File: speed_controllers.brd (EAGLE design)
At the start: 147.3 x 147.3 mm, 9 parts

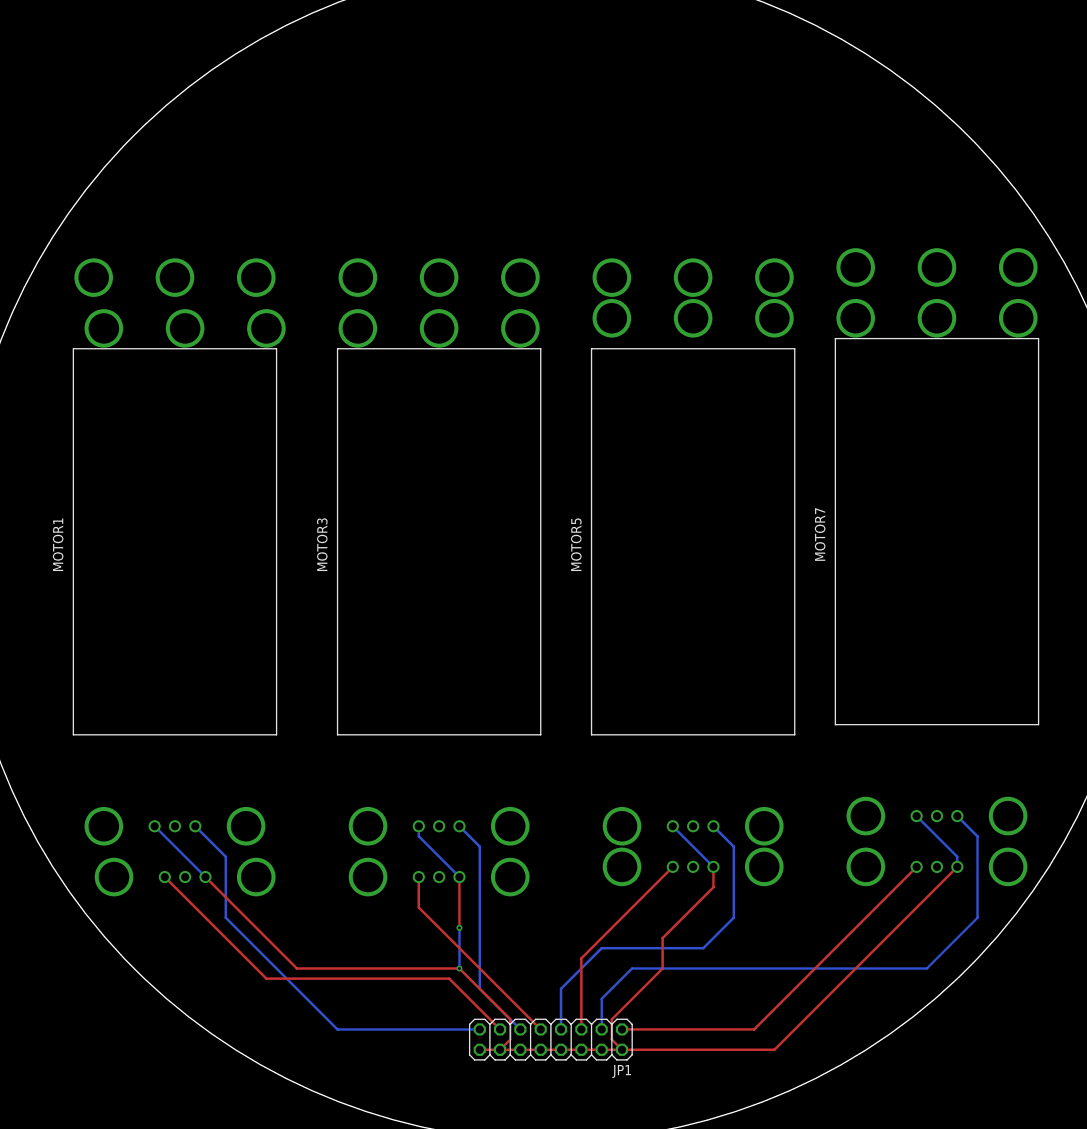
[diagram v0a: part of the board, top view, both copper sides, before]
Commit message: Redid ESC boards
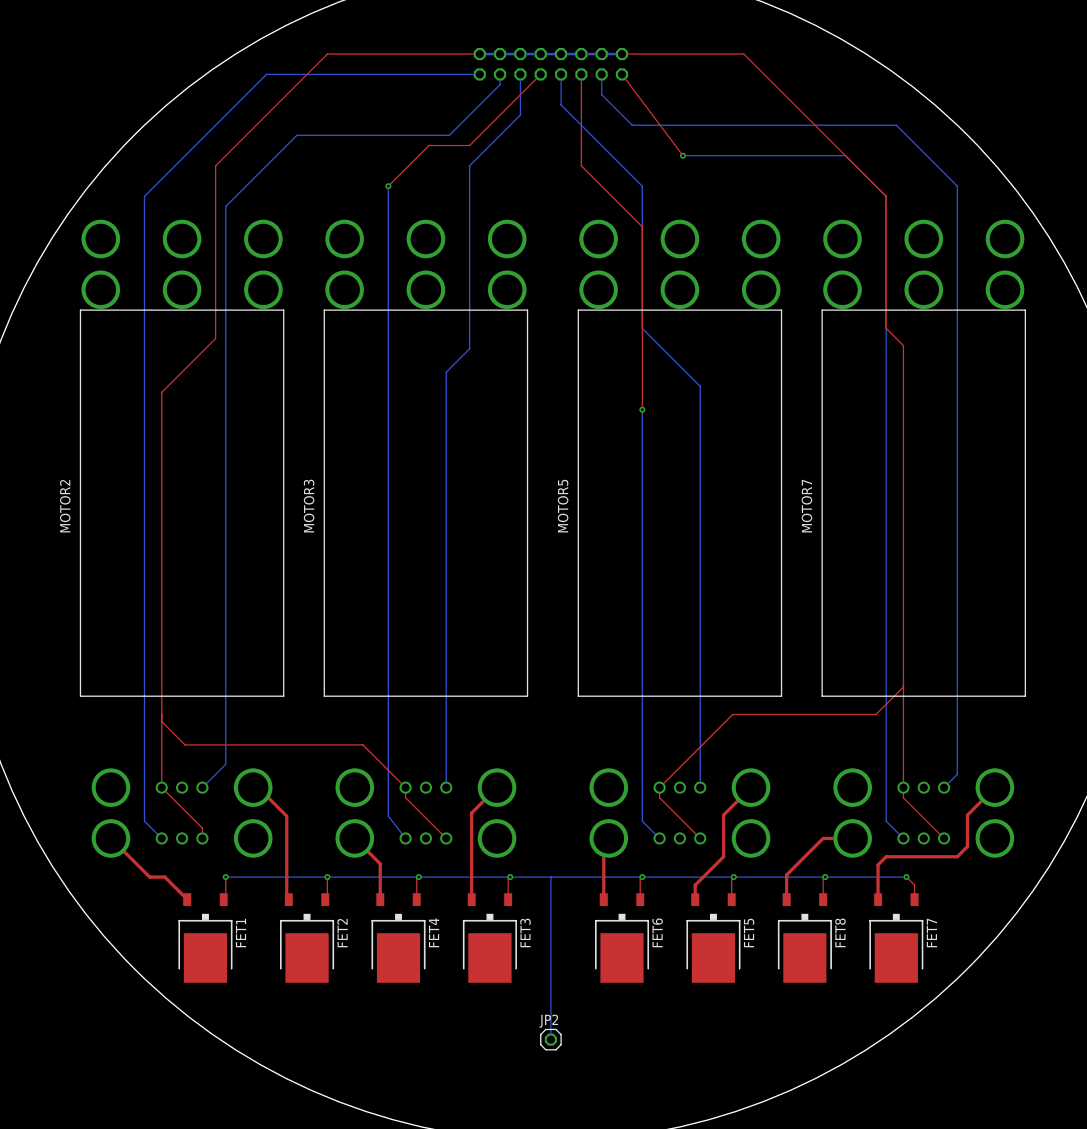
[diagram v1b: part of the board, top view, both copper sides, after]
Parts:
- added FET1, FET2, FET3, FET4, FET5, FET6, FET7, FET8: AOD403, auv:TO252
- added JP2: (no value), auv:1X01
- moved JP1 121.9 mm to (0.00, 61.0), flipped to the bottom, turned to 0 degrees
- moved MOTOR2 11.2 mm to (-46.1, 7.37), flipped to the top
- moved MOTOR4 5.10 mm to (-15.6, 1.02)
- moved MOTOR3 5.10 mm to (-15.6, 7.37)
- moved MOTOR5 5.10 mm to (16.1, 7.37)
- moved MOTOR6 3.92 mm to (16.1, 1.02)
- moved MOTOR7 3.92 mm to (46.6, 7.37)
- moved MOTOR8 3.92 mm to (46.6, 1.02)
- moved MOTOR1 1.76 mm to (-46.1, 1.02), flipped to the bottom
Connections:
- new net N$10: FET1.S, MOTOR1.VIN
- new net N$12: FET2.S, MOTOR2.VIN
- new net N$13: FET3.S, MOTOR3.VIN
- new net N$14: FET4.S, MOTOR4.VIN
- new net N$15: FET5.S, MOTOR5.VIN
- new net N$16: FET6.S, MOTOR6.VIN
- new net N$17: FET7.S, MOTOR7.VIN
- new net N$18: FET8.S, MOTOR8.VIN
- new net N$20: FET1.G, FET2.G, FET3.G, FET4.G, FET5.G, FET6.G, FET7.G, FET8.G, JP2.1
- net VCC: now also FET1.D, FET2.D, FET3.D, FET4.D, FET5.D, FET6.D, FET7.D, FET8.D; no longer MOTOR1.VIN, MOTOR2.VIN, MOTOR3.VIN, MOTOR4.VIN, MOTOR5.VIN, MOTOR6.VIN, MOTOR7.VIN, MOTOR8.VIN
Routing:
- net N$9: track 192.1 -> 357.0 mm, vias 2 -> 0
- net N$20: track 0.00 -> 129.1 mm, vias 0 -> 8
- net N$4: track 25.4 -> 107.1 mm, vias 0 -> 1
- net N$1: track 50.5 -> 129.4 mm
- net N$8: track 45.2 -> 121.4 mm, vias 0 -> 1
- net N$6: track 25.1 -> 99.6 mm, vias 0 -> 1
- net N$2: track 49.8 -> 115.7 mm
- net N$3: track 28.6 -> 93.0 mm
- net N$7: track 68.8 -> 127.6 mm
- net N$5: track 42.8 -> 96.4 mm
- net N$17: track 0.00 -> 25.3 mm
- net N$15: track 0.00 -> 16.9 mm
- net N$12: track 0.00 -> 16.2 mm
- net N$13: track 0.00 -> 15.3 mm
- net N$18: track 0.00 -> 13.2 mm
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
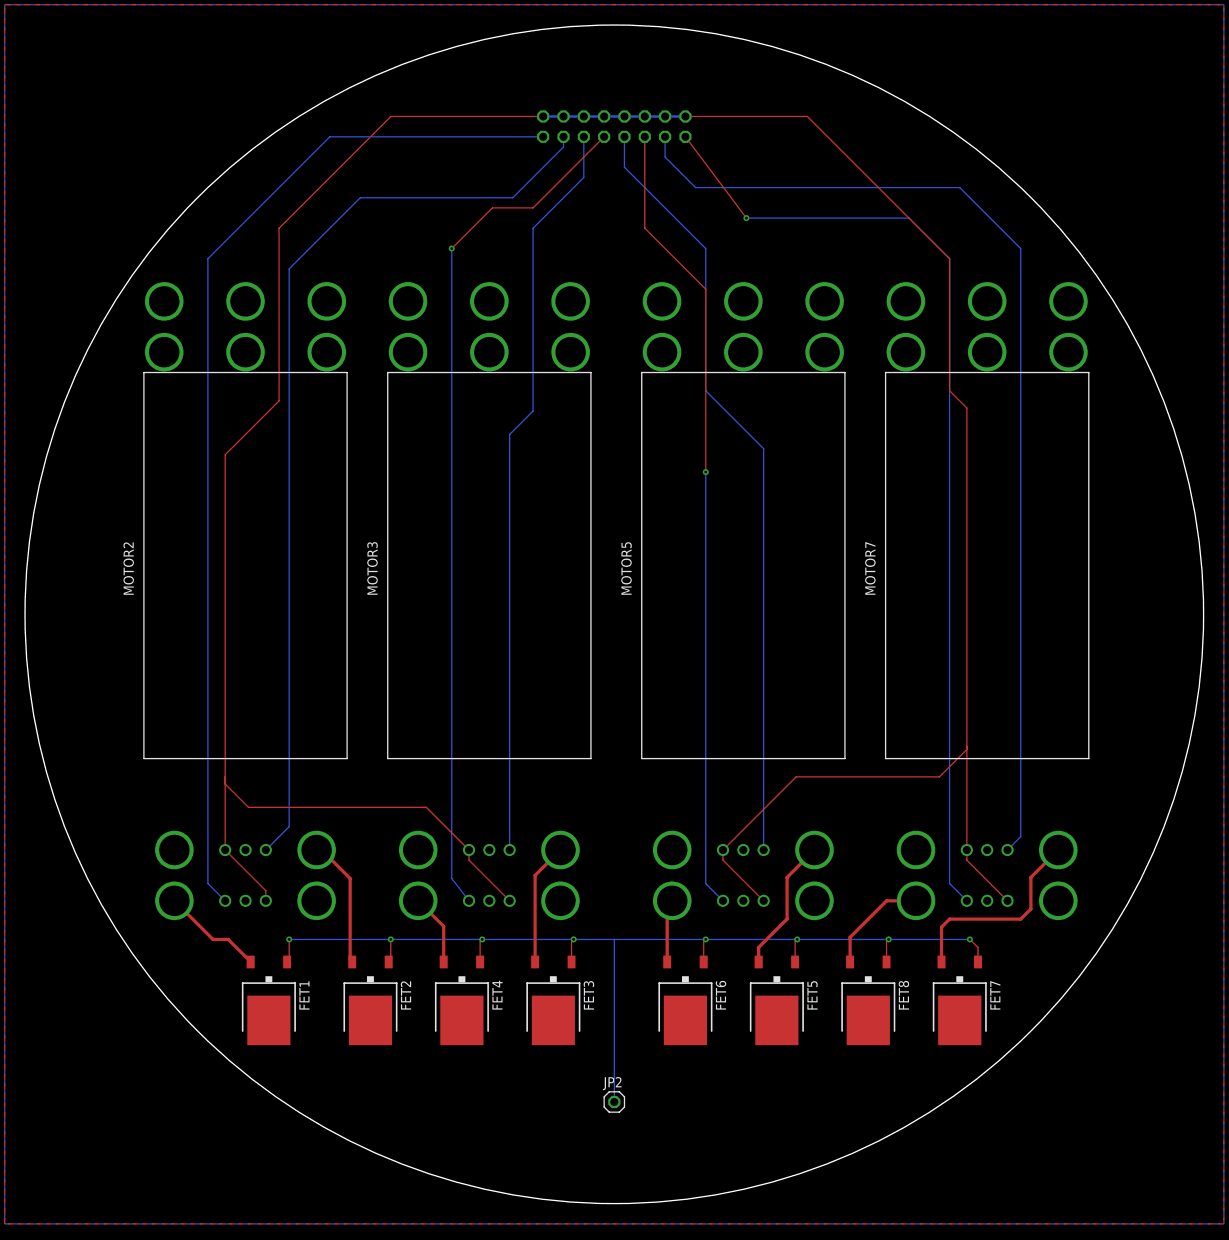
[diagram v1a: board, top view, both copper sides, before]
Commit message: ESC Board
Features:
* 8 ESC's
* XT60 battery connector P-Channel mosfets for kill switch
* Hall effect kill switch
* LED Kill switch indicators
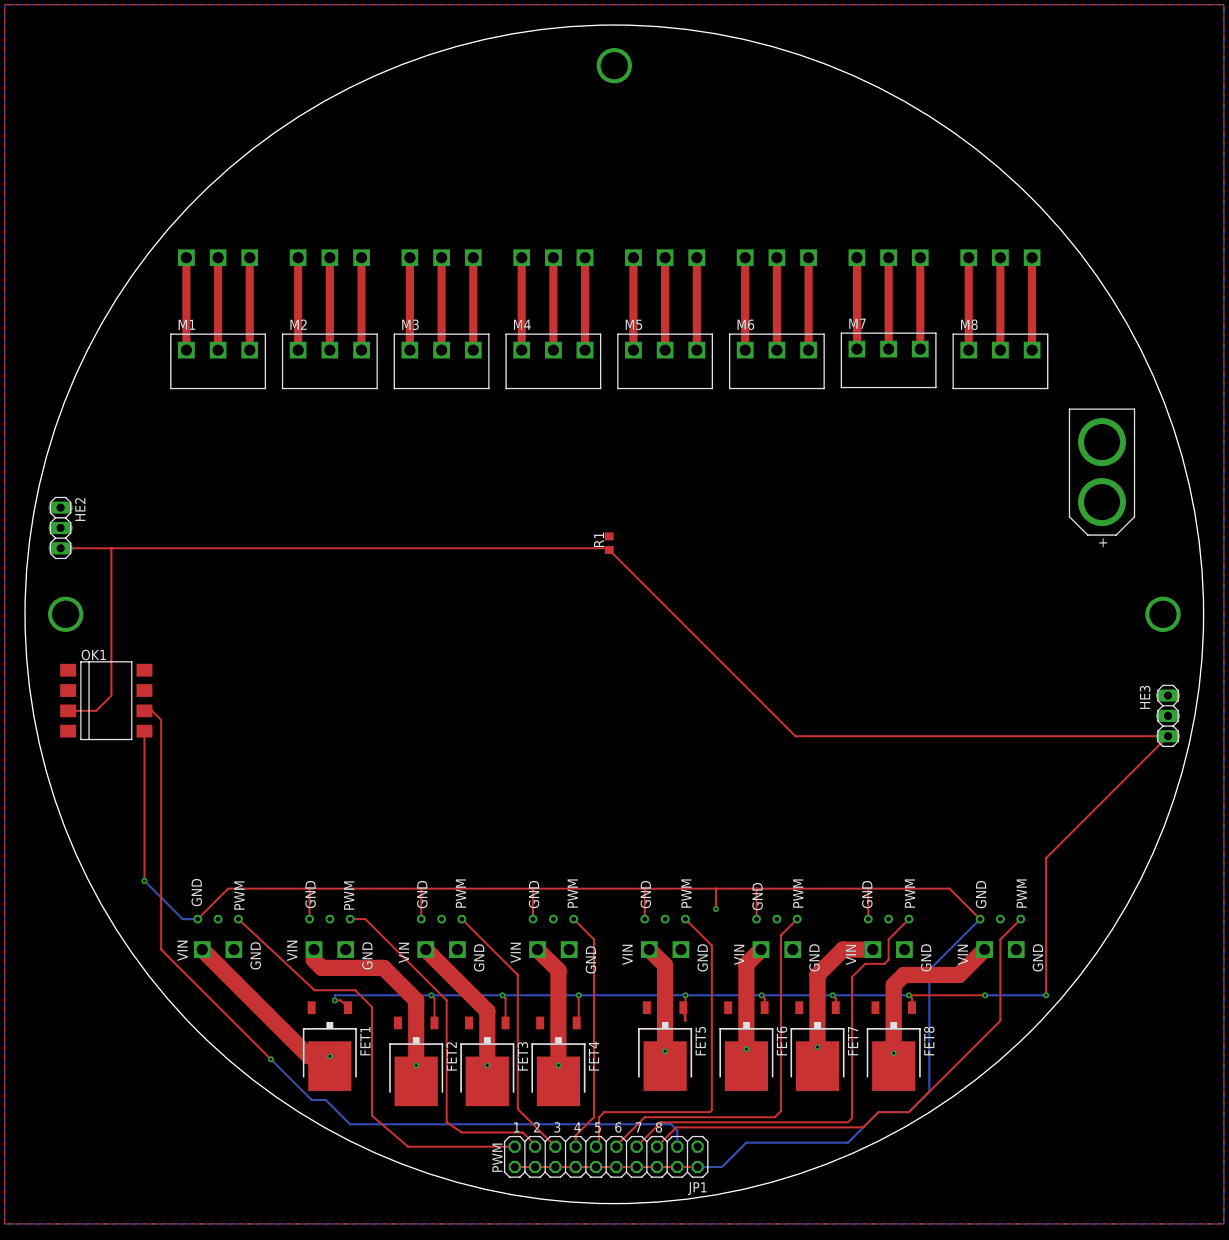
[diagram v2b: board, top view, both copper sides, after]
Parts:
- removed JP2: (no value), auv:1X01
- added HE2, HE3: (no value), auv:1X03
- added LED1, LED2, LED3, LED4, LED5, LED6, LED7, LED8: LED, auv:LED-0603
- added M1, M2, M3, M4, M5, M6, M7, M8: TE-1-1123723-3, auv:TE-1-1123723-3
- added OK1: 6N137SMD, auv:DIL8-SMD
- added R1: 10k, auv:R0603
- added R2, R3, R4, R5, R6, R7, R8, R9: 1k, auv:R0603
- added U$1: XT-60, auv:XT-60
- JP1: device auv:2X08 -> auv:2X10
- moved JP1 128.8 mm to (-1.02, -67.8), flipped to the top, turned to 180 degrees
- moved FET7 18.7 mm to (25.4, -54.0)
- moved FET5 15.1 mm to (6.35, -54.0)
- moved FET4 14.3 mm to (-6.99, -55.9)
- moved MOTOR7 13.7 mm to (34.3, 1.27), flipped to the bottom
- moved MOTOR2 12.2 mm to (-35.6, 1.27), flipped to the bottom
- moved MOTOR5 11.5 mm to (6.35, 1.27), flipped to the bottom
- moved FET3 11.2 mm to (-15.9, -55.9)
- moved FET2 9.53 mm to (-24.8, -55.9)
- moved FET6 9.53 mm to (16.5, -54.0)
- moved FET1 9.53 mm to (-35.6, -54.0)
- moved MOTOR3 8.53 mm to (-21.6, 1.27), flipped to the bottom
- moved MOTOR4 8.01 mm to (-7.62, 1.27)
- moved FET8 6.54 mm to (34.9, -54.0)
- moved MOTOR6 4.20 mm to (20.3, 1.27)
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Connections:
- removed net N$1: JP1.15, MOTOR1.PWM_SIG
- removed net N$10: FET1.S, MOTOR1.VIN
- removed net N$14: FET4.S, MOTOR4.VIN
- removed net N$15: FET5.S, MOTOR5.VIN
- removed net N$16: FET6.S, MOTOR6.VIN
- removed net N$17: FET7.S, MOTOR7.VIN
- removed net N$18: FET8.S, MOTOR8.VIN
- removed net N$2: JP1.13, MOTOR2.PWM_SIG
- removed net N$20: FET1.G, FET2.G, FET3.G, FET4.G, FET5.G, FET6.G, FET7.G, FET8.G, JP2.1
- removed net N$3: JP1.11, MOTOR3.PWM_SIG
- removed net N$4: JP1.9, MOTOR4.PWM_SIG
- removed net N$5: JP1.7, MOTOR5.PWM_SIG
- new net FET_G: FET1.G, FET2.G, FET3.G, FET4.G, FET5.G, FET6.G, FET7.G, FET8.G, HE2.3, HE3.3, OK1.3, R1.1
- new net KILL_SWITCH_OPTO: JP1.3, OK1.6
- new net M1_1: M1.1, MOTOR1.MOTOR3
- new net M1_2: M1.2, MOTOR1.MOTOR2
- new net M1_3: M1.3, MOTOR1.MOTOR1
- new net M2_1: M2.1, MOTOR2.MOTOR3
- new net M2_2: M2.2, MOTOR2.MOTOR2
- new net M2_3: M2.3, MOTOR2.MOTOR1
- new net M3_1: M3.1, MOTOR3.MOTOR3
- new net M3_2: M3.2, MOTOR3.MOTOR2
- new net M3_3: M3.3, MOTOR3.MOTOR1
- new net M4_1: M4.1, MOTOR4.MOTOR3
- new net M4_2: M4.2, MOTOR4.MOTOR2
- new net M4_3: M4.3, MOTOR4.MOTOR1
- new net M5_1: M5.1, MOTOR5.MOTOR3
- new net M5_2: M5.2, MOTOR5.MOTOR2
- new net M5_3: M5.3, MOTOR5.MOTOR1
- new net M6_1: M6.1, MOTOR6.MOTOR3
- new net M6_2: M6.2, MOTOR6.MOTOR2
- new net M6_3: M6.3, MOTOR6.MOTOR1
- new net M7_1: M7.1, MOTOR7.MOTOR3
- new net M7_2: M7.2, MOTOR7.MOTOR2
- new net M7_3: M7.3, MOTOR7.MOTOR1
- new net M8_1: M8.1, MOTOR8.MOTOR3
- new net M8_2: M8.2, MOTOR8.MOTOR2
- new net M8_3: M8.3, MOTOR8.MOTOR1
- new net N$11: LED5.C, R6.1
- new net PWM_GND: JP1.10, JP1.12, JP1.14, JP1.16, JP1.18, JP1.2, JP1.20, JP1.4, JP1.6, JP1.8, MOTOR1.PWM_GND, MOTOR2.PWM_GND, MOTOR3.PWM_GND, MOTOR4.PWM_GND, MOTOR5.PWM_GND, MOTOR6.PWM_GND, MOTOR7.PWM_GND, MOTOR8.PWM_GND, OK1.5
- new net R7: LED6.C, R7.1
- new net SIG_1: JP1.19, MOTOR1.PWM_SIG
- new net SIG_2: JP1.17, MOTOR2.PWM_SIG
- new net SIG_3: JP1.15, MOTOR3.PWM_SIG
- new net SIG_4: JP1.13, MOTOR4.PWM_SIG
- new net SIG_5: JP1.11, MOTOR5.PWM_SIG
- new net SIG_6: JP1.9, MOTOR6.PWM_SIG
- new net SIG_7: JP1.7, MOTOR7.PWM_SIG
- new net SIG_8: JP1.5, MOTOR8.PWM_SIG
- new net VIN3: FET3.D, LED3.A, MOTOR3.VIN
- new net VIN_1: FET1.D, LED1.A, MOTOR1.VIN
- new net VIN_2: FET2.D, LED2.A, MOTOR2.VIN
- new net VIN_4: FET4.D, LED4.A, MOTOR4.VIN
- new net VIN_5: FET5.D, LED5.A, MOTOR5.VIN
- new net VIN_6: FET6.D, LED6.A, MOTOR6.VIN
- new net VIN_7: FET7.D, LED7.A, MOTOR7.VIN
- new net VIN_8: FET8.D, LED8.A, MOTOR8.VIN
- net GND: now also HE2.2, HE3.2, R2.1, R3.1, R4.1, R5.1, R6.2, R7.2, R8.2, R9.2, U$1.P$2
- net N$12: now also LED7.C, R8.1; no longer FET2.S, MOTOR2.VIN
- net N$13: now also LED8.C, R9.1; no longer FET3.S, MOTOR3.VIN
- net N$6: now also LED1.C, R2.2; no longer JP1.5, MOTOR6.PWM_SIG
- net N$7: now also LED2.C, R3.2; no longer JP1.3, MOTOR7.PWM_SIG
- net N$8: now also LED3.C, R4.2; no longer JP1.1, MOTOR8.PWM_SIG
- net N$9: now also LED4.C, R5.2; no longer JP1.10, JP1.12, JP1.14, JP1.16, JP1.2, JP1.4, JP1.6, JP1.8, MOTOR1.PWM_GND, MOTOR2.PWM_GND, MOTOR3.PWM_GND, MOTOR4.PWM_GND, MOTOR5.PWM_GND, MOTOR6.PWM_GND, MOTOR7.PWM_GND, MOTOR8.PWM_GND
- net VCC: now also FET1.S, FET2.S, HE2.1, HE3.1, OK1.2, OK1.7, OK1.8, R1.2, U$1.P$1; no longer FET1.D, FET2.D, FET3.D, FET4.D, FET5.D, FET6.D, FET7.D, FET8.D
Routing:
- net N$9: track 357.0 -> 3.57 mm
- net FET_G: track 0.00 -> 323.8 mm, vias 0 -> 10
- net PWM_GND: track 0.00 -> 256.5 mm, vias 0 -> 2
- net N$1: track 129.4 -> 0.00 mm, vias 0 -> 1
- net N$20: track 129.1 -> 0.00 mm, vias 8 -> 0
- net N$7: track 127.6 -> 3.60 mm
- net N$8: track 121.4 -> 3.60 mm, vias 1 -> 0
- net N$2: track 115.7 -> 0.00 mm, vias 0 -> 1
- net KILL_SWITCH_OPTO: track 0.00 -> 107.2 mm, vias 0 -> 1
- net N$4: track 107.1 -> 0.00 mm, vias 1 -> 0
- net N$5: track 96.4 -> 0.00 mm
- net N$6: track 99.6 -> 3.82 mm, vias 1 -> 0
- net N$3: track 93.0 -> 0.00 mm, vias 0 -> 1
- net SIG_8: track 0.00 -> 63.2 mm
- net SIG_7: track 0.00 -> 57.6 mm
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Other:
- board text added: "+"
- board text added: "1"
- board text added: "2"
- board text added: "3"
- board text added: "4"
- board text added: "5"
- board text added: "6"
- board text added: "7"
- board text added: "8"
- board text added: "GND"
- board text added: "PWM"
- board text added: "VIN"
